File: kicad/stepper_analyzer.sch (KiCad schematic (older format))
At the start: 38 parts, among them J1 Connector_Conn_01x04_Male, J2 Connector_Conn_01x04_Male, J3 Conn_01x01, M1 Motor, Q1 SI2301, SW1 switch, SW2 switch, U1 ACS70331EOLCTR-2P5B3, U2 ACS70331EOLCTR-2P5B3, U3 Pico

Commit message: Cleaned up the schematic. No semantic change.
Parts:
- FPC2: symbol Connector:Conn_01x06_Female -> stepper_motor_analyzer:Conn_01x06_Female
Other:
- note added: "Capacitive touch FT6236 I2C,\n0.5mm pitch FPC, BOTTOM contacts."
- note added: "Simple Stepper Motor Analyzer (Pico based)"
- note added: "TFT 320x480 ILI9488 16bit data.\n0.5mm pitch FPC, TOP contacts."
- note removed: "Capacitive touch FT6236 I2C,\n0.5mm pitch, BOTTOM contacts."
- note removed: "Simple Stepper Motor Analyzer Mk2"
- note removed: "TFT 320x480 ILI9488 16bit data.\n0.5mm pitch, TOP contacts."
- moved on the sheet: C3, C4, D1, D2, D3, FPC1, J3, Q1, R1, R2, R3, R4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

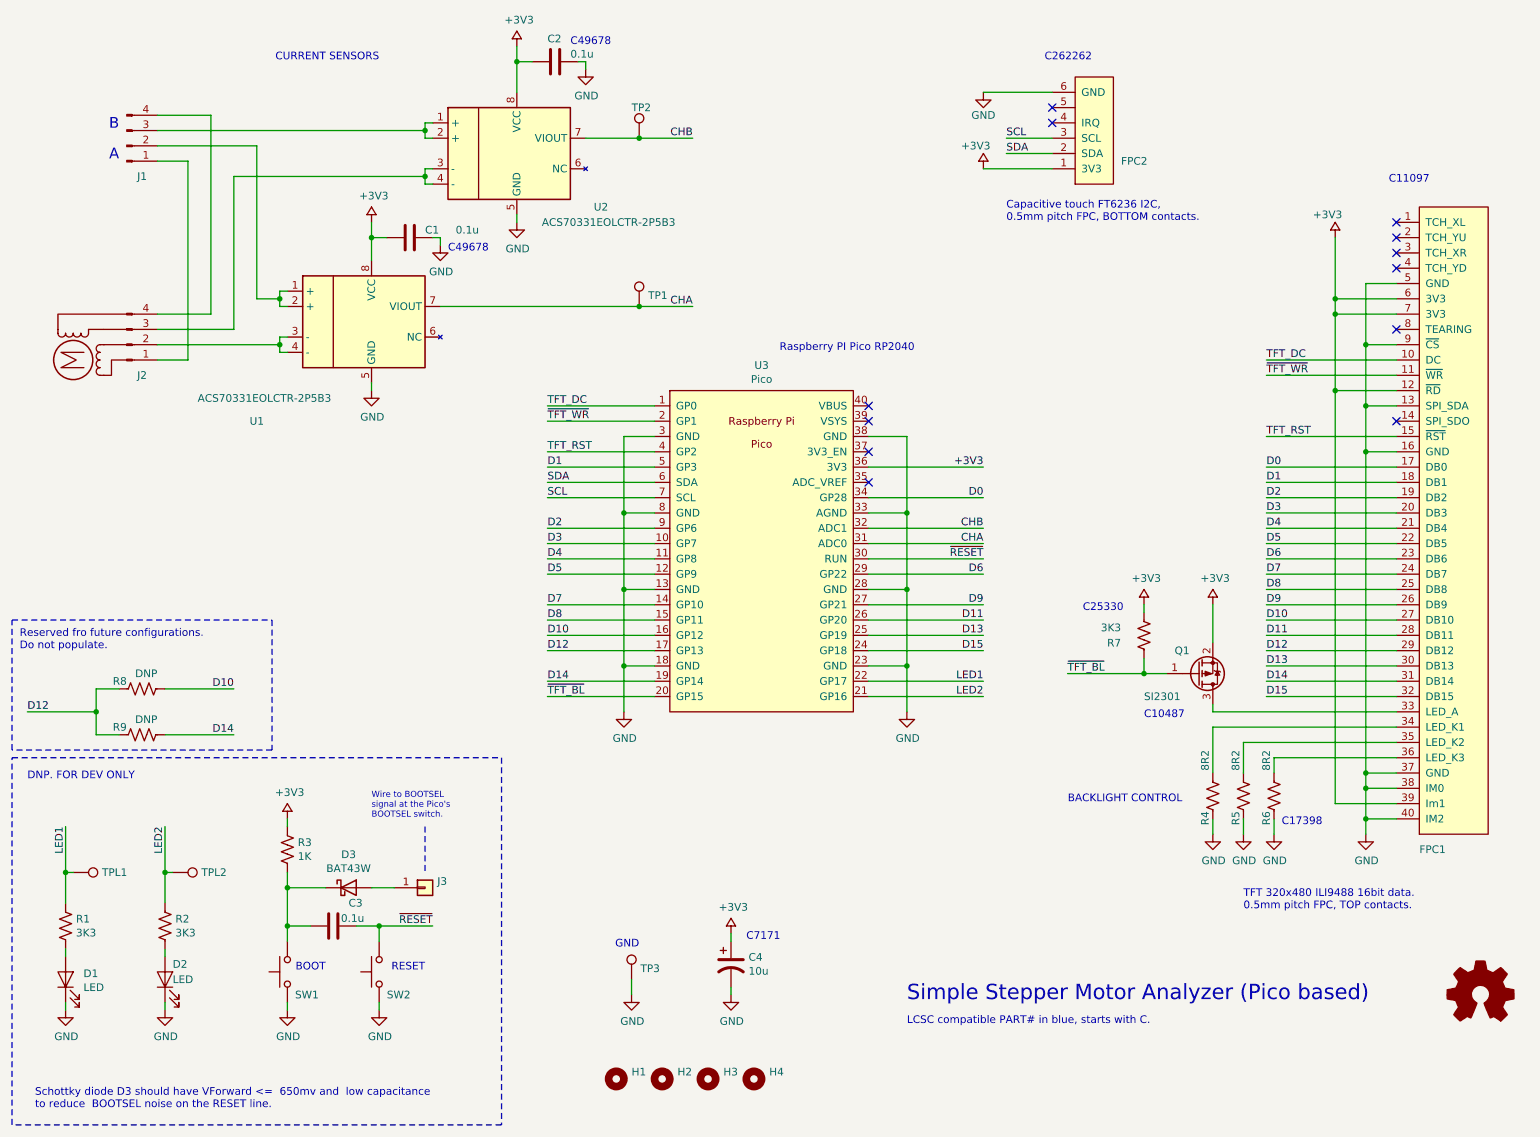
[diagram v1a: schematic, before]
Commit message: Updated kicad files for MK3
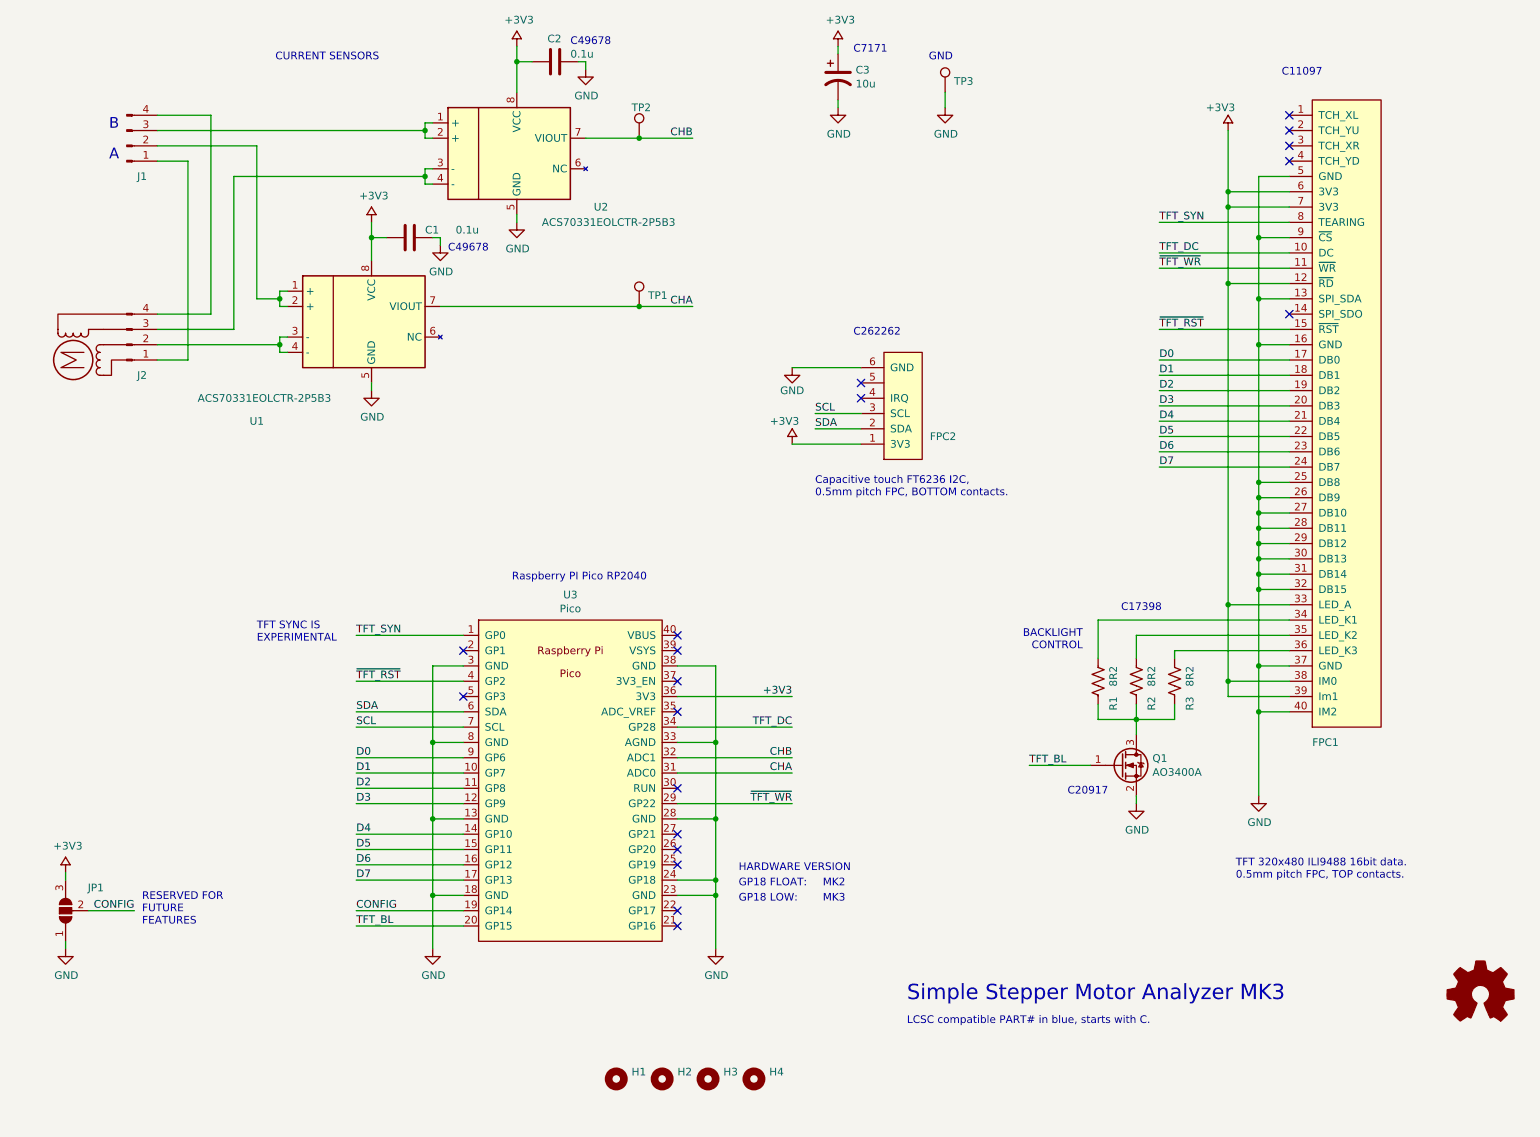
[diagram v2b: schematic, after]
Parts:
- removed C3: 0.1u, stepper_motor_analyzer:C_0805_2012Metric_Pad1.15x1.40mm_HandSolder_no_3d, symbol Device:C
- removed D1, D2: LED, stepper_motor_analyzer:LED_0805_2012Metric_Pad1.15x1.40mm_HandSolder_double_side_no_3d, symbol stepper_motor_analyzer:LED
- removed D3: BAT43W, stepper_motor_analyzer:D_SOD-123_no_3d, symbol Device:D_Schottky
- removed J3: Conn_01x01, stepper_motor_analyzer:SolderWire-0.1sqmm_1x01_D0.4mm_OD1mm, symbol Connector_Generic:Conn_01x01
- removed Q1: SI2301, stepper_motor_analyzer:SOT-23_hand_soldering, symbol Transistor_FET:Si2371EDS
- removed R1, R2: 3K3, stepper_motor_analyzer:R_0805_2012Metric_Pad1.15x1.40mm_HandSolder_no_3d, symbol Device:R_US
- removed R3: 1K, stepper_motor_analyzer:R_0805_2012Metric_Pad1.15x1.40mm_HandSolder_no_3d, symbol Device:R_US
- removed R7: 3K3, stepper_motor_analyzer:R_0805_2012Metric_Pad1.15x1.40mm_HandSolder, symbol Device:R_US
- removed R8, R9: DNP, stepper_motor_analyzer:R_0805_2012Metric_Pad1.15x1.40mm_HandSolder_no_3d, symbol Device:R_US
- removed SW1, SW2: switch, stepper_motor_analyzer:SW_Push_1P1T_NO_CK_KMR2_double_size_no_3d, symbol stepper_motor_analyzer:switch
- removed TPL1, TPL2: TestPoint, stepper_motor_analyzer:testpoint_double_side, symbol stepper_motor_analyzer:TestPoint
- added JP1: SolderJumper_3_Open, Jumper:SolderJumper-3_P1.3mm_Open_Pad1.0x1.5mm_NumberLabels, symbol stepper_motor_analyzer:SolderJumper_3_Open
- added Q1: AO3400A, Package_TO_SOT_SMD:SOT-23, symbol Transistor_FET:AO3400A
- R1: renamed from R4; LCSC C17398 -> C25330
- R2: renamed from R5; LCSC C17398 -> C25330
- R3: renamed from R6; LCSC C17398 -> C25330
- renumbered C4 to C3
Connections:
- net D15 is gone; now on net GND: FPC1.32 (DB15), U3.24 (GP18)
- net +3V3: now also FPC1.33 (LED_A), FPC1.38 (IM0), JP1.3 (B)
- net D0: now also U3.9 (GP6); no longer U3.34 (GP28)
- net D1: now also U3.10 (GP7); no longer U3.5 (GP3)
- net D2: now also U3.11 (GP8); no longer U3.9 (GP6)
- net D3: now also U3.12 (GP9); no longer U3.10 (GP7)
- net D4: now also U3.14 (GP10); no longer U3.11 (GP8)
- net D5: now also U3.15 (GP11); no longer U3.12 (GP9)
- net D6: now also U3.16 (GP12); no longer U3.29 (GP22)
- net D7: now also U3.17 (GP13); no longer U3.14 (GP10)
- net GND: now also FPC1.25 (DB8), FPC1.26 (DB9), FPC1.27 (DB10), FPC1.28 (DB11), FPC1.29 (DB12), FPC1.30 (DB13), FPC1.31 (DB14), JP1.1 (A), Q1.2 (S); no longer FPC1.38 (IM0), R1.1, R2.1, R3.1
- net TFT_DC: now also U3.34 (GP28); no longer U3.1 (GP0)
- net ~TFT_WR: now also U3.29 (GP22); no longer U3.2 (GP1)
- net TFT_SYN: now reaches FPC1.8 (TEARING)
- net TFT_SYN: now also U3.1 (GP0)
- removed net D10: FPC1.27 (DB10), U3.16 (GP12)
- net D11: no longer names the net of U3.26 (GP20)
- net D11: no longer FPC1.28 (DB11)
- removed net D12: FPC1.29 (DB12), U3.17 (GP13)
- net D13: no longer names the net of U3.25 (GP19)
- net D13: no longer FPC1.30 (DB13)
- net D14 renamed CONFIG
- net CONFIG: now also JP1.2 (C); no longer FPC1.31 (DB14)
- removed net D8: FPC1.25 (DB8), U3.15 (GP11)
- net D9: no longer names the net of U3.27 (GP21)
- net D9: no longer FPC1.26 (DB9)
- net LED1: no longer names the net of U3.22 (GP17)
- net LED2: no longer names the net of U3.21 (GP16)
- net TFT_RST renamed ~TFT_RST
- net ~RESET: no longer names the net of U3.30 (RUN)
- net ~TFT_BL renamed TFT_BL
- net TFT_BL: now also Q1.1 (G)
- new net: Q1.3 (D), R1.1, R2.1, R3.1
- no-connect marks 12 -> 19
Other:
- note added: "BACKLIGHT\nCONTROL"
- note added: "C20917"
- note added: "GP18 FLOAT:"
- note added: "GP18 LOW:"
- note added: "HARDWARE VERSION"
- note added: "MK2"
- note added: "MK3"
- note added: "RESERVED FOR\nFUTURE\nFEATURES"
- note added: "Simple Stepper Motor Analyzer MK3"
- note added: "TFT SYNC IS\nEXPERIMENTAL"
- note removed: "BACKLIGHT CONTROL"
- note removed: "BOOT"
- note removed: "C10487"
- note removed: "C25330"
- note removed: "DNP. FOR DEV ONLY"
- note removed: "RESET"
- note removed: "Reserved fro future configurations.\nDo not populate."
- note removed: "Schottky diode D3 should have VForward <= 650mv and low capacitance\nto reduce BOOTSEL noise on the RESET line.\n"
- note removed: "Simple Stepper Motor Analyzer (Pico based)"
- note removed: "Wire to BOOTSEL\nsignal at the Pico's\nBOOTSEL switch."
- moved on the sheet: C3, FPC1, FPC2, R1, R2, R3, TP3, U3

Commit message: Updated label on the PCB.
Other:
- note added: "Capacitive touch FT6206 I2C,\n0.5mm pitch FPC, BOTTOM contacts."
- note removed: "Capacitive touch FT6236 I2C,\n0.5mm pitch FPC, BOTTOM contacts."
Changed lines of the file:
@@
 TFT 320x480 ILI9488 16bit data.\n0.5mm pitch FPC, TOP contacts.
 Text Notes 5800 3850 0    50   ~ 0
-Capacitive touch FT6236 I2C,\n0.5mm pitch FPC, BOTTOM contacts.
+Capacitive touch FT6206 I2C,\n0.5mm pitch FPC, BOTTOM contacts.
 Text Notes 4700 4400 2    50   ~ 0
 Raspberry PI Pico RP2040

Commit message: Remove A,B test points. Reduce bottom layer traces.
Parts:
- removed TP1, TP2: TestPoint, stepper_motor_analyzer:testpoint_one_side, symbol stepper_motor_analyzer:TestPoint
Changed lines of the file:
@@
 Wire Wire Line
 	3850 2000 3850 2050
-$Comp
-L stepper_motor_analyzer:TestPoint TP2
-U 1 1 60A27A27
-P 4650 1500
-F 0 "TP2" H 4600 1700 50  0000 L CNN
-F 1 "TestPoint" H 4708 1527 50  0001 L CNN
-F 2 "stepper_motor_analyzer:testpoint_one_side" H 4850 1500 50  0001 C CNN
-F 3 "" H 4850 1500 50  0001 C CNN
-	1    4650 1500
-	1    0    0    -1
-$EndComp
-Wire Wire Line
-	4300 1500 4650 1500
-Connection ~ 4650 1500
-Wire Wire Line
-	4650 1500 5000 1500
 Text Label 5000 1500 2    50   ~ 0
 CHB
@@
 	2900 3150 2900 3100
 Wire Wire Line
-	3350 2600 4650 2600
-Wire Wire Line
 	2900 2300 2900 2150
 $Comp
@@
 Wire Wire Line
 	1500 1550 2150 1550
-$Comp
-L stepper_motor_analyzer:TestPoint TP1
-U 1 1 60B0FCCE
-P 4650 2600
-F 0 "TP1" H 4708 2672 50  0000 L CNN
-F 1 "TestPoint" H 4708 2627 50  0001 L CNN
-F 2 "stepper_motor_analyzer:testpoint_one_side" H 4850 2600 50  0001 C CNN
-F 3 "" H 4850 2600 50  0001 C CNN
-	1    4650 2600
-	1    0    0    -1
-$EndComp
-Connection ~ 4650 2600
-Wire Wire Line
-	4650 2600 5000 2600
 Text Label 5000 2600 2    50   ~ 0
 CHA
@@
 Text Notes 7450 5800 0    50   ~ 0
 C20917
+Wire Wire Line
+	4300 1500 5000 1500
+Wire Wire Line
+	3350 2600 5000 2600
 $EndSCHEMATC
